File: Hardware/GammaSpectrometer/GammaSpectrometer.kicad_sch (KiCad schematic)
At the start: 0 parts

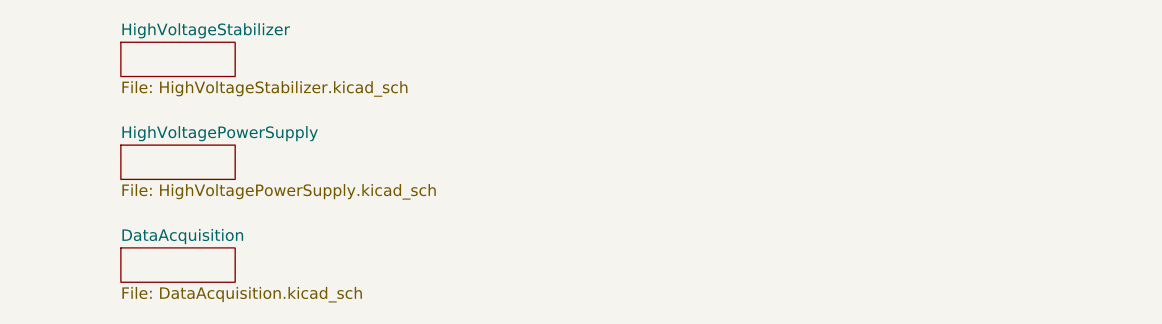
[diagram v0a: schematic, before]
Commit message: fixed footprints
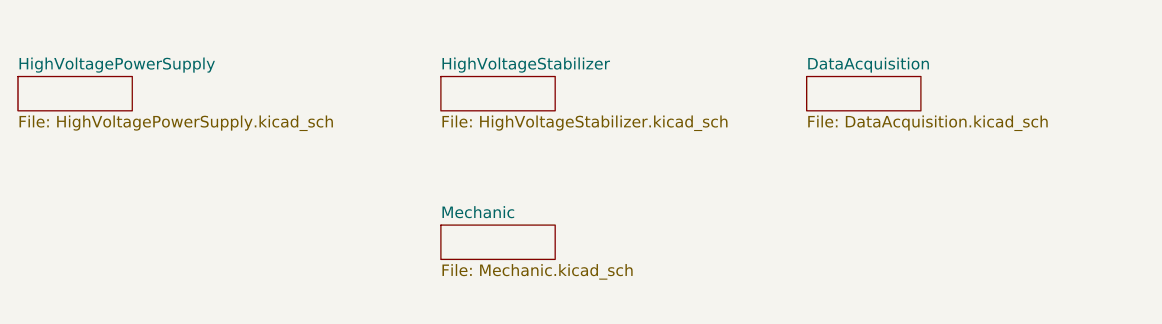
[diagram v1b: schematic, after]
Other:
- added sheet Mechanic (Mechanic.kicad_sch)
